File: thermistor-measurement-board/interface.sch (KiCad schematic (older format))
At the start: 12 parts, among them P401 PWR, P402 BIAS, P403 OUT_A, P404 OUT_B, P406 I/O

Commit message: took care of a few board review tasks
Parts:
- added P405: ADC_REF, Pin_Headers:Pin_Header_Straight_1x02, symbol CONN_01X02
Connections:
- new net ADC_REF+: P405.1 (P1)
- new net ADC_REF-: P405.2 (P2)
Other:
- moved on the sheet: P403, P404, P406

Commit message: lots of design review and related fixes/improvements
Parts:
- P405: footprint Pin_Headers:Pin_Header_Straight_1x02 -> Pin_Headers:Pin_Header_Straight_1x04; symbol CONN_01X02 -> CONN_01X04
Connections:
- net ADC_REF+: now also P405.2 (P2)
- net ADC_REF-: now also P405.3 (P3), P405.4 (P4); no longer P405.2 (P2)
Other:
- moved on the sheet: P403, P404, P406
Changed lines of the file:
@@
 	3500 1500 2900 1500
 Wire Wire Line
-	2650 4300 3250 4300
-Wire Wire Line
-	2650 4400 3250 4400
-Wire Wire Line
 	2650 4500 3250 4500
-Text Label 2650 4300 0    60   ~ 0
+Wire Wire Line
+	2650 4600 3250 4600
+Wire Wire Line
+	2650 4700 3250 4700
+Text Label 2650 4500 0    60   ~ 0
 SCLK
-Text Label 2650 4500 0    60   ~ 0
+Text Label 2650 4700 0    60   ~ 0
 MISO
-Text Label 2650 4400 0    60   ~ 0
+Text Label 2650 4600 0    60   ~ 0
 MOSI
-Text Label 3500 2900 2    60   ~ 0
+Text Label 3500 3100 2    60   ~ 0
 OUT_A+
-Text Label 3500 3100 2    60   ~ 0
+Text Label 3500 3300 2    60   ~ 0
 OUT_A-
 Wire Wire Line
-	2900 3100 3500 3100
-Wire Wire Line
-	3500 2900 2900 2900
+	2900 3300 3500 3300
+Wire Wire Line
+	3500 3100 2900 3100
 $Comp
 L GND #PWR038
 U 1 1 56B76BAA
-P 2750 3900
-F 0 "#PWR038" H 2750 3650 50  0001 C CNN
-F 1 "GND" H 2750 3750 50  0000 C CNN
-F 2 "" H 2750 3900 50  0000 C CNN
-F 3 "" H 2750 3900 50  0000 C CNN
-	1    2750 3900
+P 2750 4100
+F 0 "#PWR038" H 2750 3850 50  0001 C CNN
+F 1 "GND" H 2750 3950 50  0000 C CNN
+F 2 "" H 2750 4100 50  0000 C CNN
+F 3 "" H 2750 4100 50  0000 C CNN
+	1    2750 4100
 	0    1    -1   0
 $EndComp
 Wire Wire Line
-	3250 3900 2750 3900
-Wire Wire Line
-	2650 4200 3250 4200
-Text Label 2650 4200 0    60   ~ 0
+	3250 4100 2750 4100
+Wire Wire Line
+	2650 4400 3250 4400
+Text Label 2650 4400 0    60   ~ 0
 MUX_CS
-Text Label 4350 4000 2    60   ~ 0
+Text Label 4350 4200 2    60   ~ 0
 ADC_CS
 Wire Wire Line
-	4350 4000 3750 4000
-Wire Wire Line
-	2650 4100 3250 4100
-Text Label 2650 4100 0    60   ~ 0
+	4350 4200 3750 4200
+Wire Wire Line
+	2650 4300 3250 4300
+Text Label 2650 4300 0    60   ~ 0
 MUX_EN
+Text Label 4350 4300 2    60   ~ 0
+ADC_DR_INT
+Wire Wire Line
+	3750 4300 4350 4300
 Text Label 4350 4100 2    60   ~ 0
-ADC_DR_INT
-Wire Wire Line
-	3750 4100 4350 4100
-Text Label 4350 3900 2    60   ~ 0
 ADC_RST
 Wire Wire Line
-	4350 3900 3750 3900
+	4350 4100 3750 4100
 Text Label 7000 1100 2    60   ~ 0
 AVCC
@@
 Wire Wire Line
 	1700 3500 1100 3500
-Text Label 3500 3400 2    60   ~ 0
+Text Label 3500 3600 2    60   ~ 0
 OUT_B+
-Text Label 3500 3600 2    60   ~ 0
+Text Label 3500 3800 2    60   ~ 0
 OUT_B-
 Wire Wire Line
-	2900 3600 3500 3600
-Wire Wire Line
-	3500 3400 2900 3400
+	2900 3800 3500 3800
+Wire Wire Line
+	3500 3600 2900 3600
 $Comp
 L CONN_01X03 P403
 U 1 1 56B95AC0
-P 2700 3000
-F 0 "P403" H 2700 3200 50  0000 C CNN
-F 1 "OUT_A" V 2800 3000 50  0000 C CNN
-F 2 "Pin_Headers:Pin_Header_Straight_1x03" H 2700 3000 50  0001 C CNN
-F 3 "" H 2700 3000 50  0000 C CNN
-	1    2700 3000
+P 2700 3200
+F 0 "P403" H 2700 3400 50  0000 C CNN
+F 1 "OUT_A" V 2800 3200 50  0000 C CNN
+F 2 "Pin_Headers:Pin_Header_Straight_1x03" H 2700 3200 50  0001 C CNN
+F 3 "" H 2700 3200 50  0000 C CNN
+	1    2700 3200
 	-1   0    0    -1
 $EndComp
@@
 L CONN_01X03 P404
 U 1 1 56B95B06
-P 2700 3500
-F 0 "P404" H 2700 3700 50  0000 C CNN
-F 1 "OUT_B" V 2800 3500 50  0000 C CNN
-F 2 "Pin_Headers:Pin_Header_Straight_1x03" H 2700 3500 50  0001 C CNN
-F 3 "" H 2700 3500 50  0000 C CNN
-	1    2700 3500
+P 2700 3700
+F 0 "P404" H 2700 3900 50  0000 C CNN
+F 1 "OUT_B" V 2800 3700 50  0000 C CNN
+F 2 "Pin_Headers:Pin_Header_Straight_1x03" H 2700 3700 50  0001 C CNN
+F 3 "" H 2700 3700 50  0000 C CNN
+	1    2700 3700
 	-1   0    0    -1
 $EndComp
 Wire Wire Line
-	4350 4200 3750 4200
-Text Label 4350 4200 2    60   ~ 0
+	4350 4400 3750 4400
+Text Label 4350 4400 2    60   ~ 0
 AMP_MUX_CS
 Wire Wire Line
-	4350 4300 3750 4300
-Text Label 4350 4300 2    60   ~ 0
+	4350 4500 3750 4500
+Text Label 4350 4500 2    60   ~ 0
 AMP_MUX_EN
 Wire Wire Line
-	2650 4000 3250 4000
+	2650 4200 3250 4200
 Text HLabel 1100 4300 0    60   Output ~ 0
 AMP_MUX_CS
@@
 L CONN_02X07 P406
 U 1 1 56B9EC32
-P 3500 4200
-F 0 "P406" H 3500 4600 50  0000 C CNN
-F 1 "I/O" V 3500 4200 50  0000 C CNN
-F 2 "Pin_Headers:Pin_Header_Straight_2x07" H 3500 3000 50  0001 C CNN
-F 3 "" H 3500 3000 50  0000 C CNN
-	1    3500 4200
-	1    0    0    -1
-$EndComp
-Text Label 2650 4000 0    60   ~ 0
+P 3500 4400
+F 0 "P406" H 3500 4800 50  0000 C CNN
+F 1 "I/O" V 3500 4400 50  0000 C CNN
+F 2 "Pin_Headers:Pin_Header_Straight_2x07" H 3500 3200 50  0001 C CNN
+F 3 "" H 3500 3200 50  0000 C CNN
+	1    3500 4400
+	1    0    0    -1
+$EndComp
+Text Label 2650 4200 0    60   ~ 0
 ADC_MCLK
 $Comp
 L GND #PWR041
 U 1 1 56B9EE11
-P 4250 4500
-F 0 "#PWR041" H 4250 4250 50  0001 C CNN
-F 1 "GND" H 4250 4350 50  0000 C CNN
-F 2 "" H 4250 4500 50  0000 C CNN
-F 3 "" H 4250 4500 50  0000 C CNN
-	1    4250 4500
+P 4250 4700
+F 0 "#PWR041" H 4250 4450 50  0001 C CNN
+F 1 "GND" H 4250 4550 50  0000 C CNN
+F 2 "" H 4250 4700 50  0000 C CNN
+F 3 "" H 4250 4700 50  0000 C CNN
+	1    4250 4700
 	0    -1   1    0
 $EndComp
 Wire Wire Line
-	3750 4500 4250 4500
-Text Label 4350 4400 2    60   ~ 0
+	3750 4700 4250 4700
+Text Label 4350 4600 2    60   ~ 0
 DVDD
 Wire Wire Line
-	4350 4400 3750 4400
+	4350 4600 3750 4600
 $Comp
 L PWR_FLAG #FLG042
@@
 Wire Wire Line
 	1700 2600 1100 2600
-Text Label 3500 3500 2    60   ~ 0
+Text Label 3500 3700 2    60   ~ 0
 REF_B
-Text Label 3500 3000 2    60   ~ 0
+Text Label 3500 3200 2    60   ~ 0
 REF_A
 Wire Wire Line
-	3500 3500 2900 3500
-Wire Wire Line
-	3500 3000 2900 3000
+	3500 3700 2900 3700
+Wire Wire Line
+	3500 3200 2900 3200
 Text Label 1700 1800 2    60   ~ 0
 VS_BIAS
@@
 	1700 2900 1100 2900
 $Comp
-L CONN_01X02 P405
+L CONN_01X04 P405
 U 1 1 56BCEDCB
-P 2700 2450
-F 0 "P405" H 2700 2600 50  0000 C CNN
-F 1 "ADC_REF" V 2800 2450 50  0000 C CNN
-F 2 "Pin_Headers:Pin_Header_Straight_1x02" H 2700 2450 50  0001 C CNN
-F 3 "" H 2700 2450 50  0000 C CNN
-	1    2700 2450
+P 2700 2550
+F 0 "P405" H 2700 2800 50  0000 C CNN
+F 1 "ADC_REF" V 2800 2550 50  0000 C CNN
+F 2 "Pin_Headers:Pin_Header_Straight_1x04" H 2700 2550 50  0001 C CNN
+F 3 "" H 2700 2550 50  0000 C CNN
+	1    2700 2550
 	-1   0    0    -1
 $EndComp
 Text Label 3500 2400 2    60   ~ 0
 ADC_REF+
-Text Label 3500 2500 2    60   ~ 0
+Text Label 3500 2700 2    60   ~ 0
 ADC_REF-
 Wire Wire Line
-	3500 2400 2900 2400
-Wire Wire Line
-	2900 2500 3500 2500
+	2900 2500 3000 2500
+Wire Wire Line
+	3000 2500 3000 2400
+Connection ~ 3000 2400
+Wire Wire Line
+	2900 2600 3000 2600
+Wire Wire Line
+	3000 2600 3000 2700
+Connection ~ 3000 2700
+Wire Wire Line
+	2900 2400 3500 2400
+Wire Wire Line
+	2900 2700 3500 2700
 $EndSCHEMATC

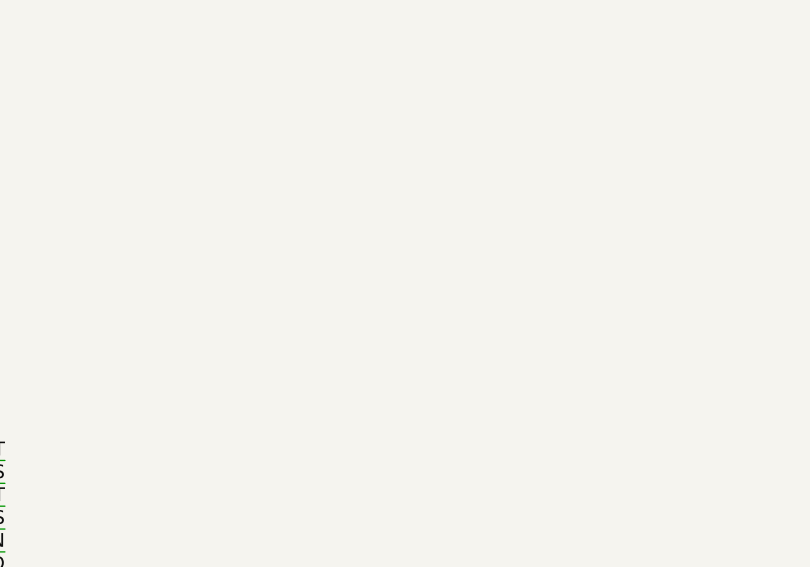
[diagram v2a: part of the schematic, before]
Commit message: read a million instrument amp datasheets and found one that should work nicely for low gain.
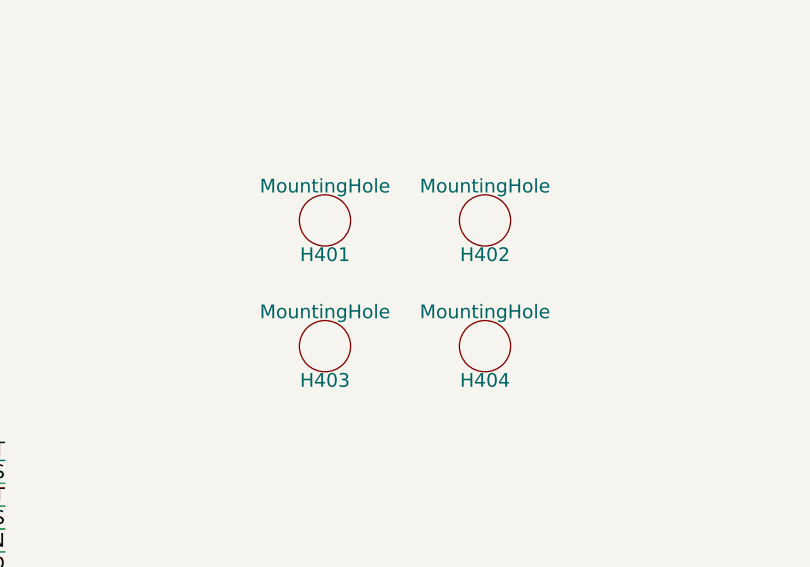
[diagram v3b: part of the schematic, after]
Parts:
- added H401, H402, H403, H404: MountingHole, MountingHole_2-5mm, symbol MountingHole
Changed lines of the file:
@@
 $Descr A4 11693 8268
 encoding utf-8
-Sheet 4 4
+Sheet 4 5
 Title ""
 Date ""
@@
 	1100 800  1700 800
 $Comp
-L GND #PWR033
+L GND #PWR035
 U 1 1 56B64614
 P 1700 1400
-F 0 "#PWR033" H 1700 1150 50  0001 C CNN
+F 0 "#PWR035" H 1700 1150 50  0001 C CNN
 F 1 "GND" H 1700 1250 50  0000 C CNN
 F 2 "" H 1700 1400 50  0000 C CNN
@@
 $EndComp
 $Comp
-L GNDA #PWR034
+L GNDA #PWR036
 U 1 1 56B6461A
 P 1700 1600
-F 0 "#PWR034" H 1700 1350 50  0001 C CNN
+F 0 "#PWR036" H 1700 1350 50  0001 C CNN
 F 1 "GNDA" H 1700 1450 50  0000 C CNN
 F 2 "" H 1700 1600 50  0000 C CNN
@@
 $EndComp
 $Comp
-L GND #PWR035
+L GND #PWR037
 U 1 1 56B765F3
 P 5200 1600
-F 0 "#PWR035" H 5200 1350 50  0001 C CNN
+F 0 "#PWR037" H 5200 1350 50  0001 C CNN
 F 1 "GND" H 5200 1450 50  0000 C CNN
 F 2 "" H 5200 1600 50  0000 C CNN
@@
 $EndComp
 $Comp
-L GNDA #PWR036
+L GNDA #PWR038
 U 1 1 56B7660A
 P 6100 1600
-F 0 "#PWR036" H 6100 1350 50  0001 C CNN
+F 0 "#PWR038" H 6100 1350 50  0001 C CNN
 F 1 "GNDA" H 6100 1450 50  0000 C CNN
 F 2 "" H 6100 1600 50  0000 C CNN
@@
 	3300 800  2900 800
 $Comp
-L GNDA #PWR037
+L GNDA #PWR039
 U 1 1 56B767B9
 P 3400 1400
-F 0 "#PWR037" H 3400 1150 50  0001 C CNN
+F 0 "#PWR039" H 3400 1150 50  0001 C CNN
 F 1 "GNDA" H 3400 1250 50  0000 C CNN
 F 2 "" H 3400 1400 50  0000 C CNN
@@
 	3500 3100 2900 3100
 $Comp
-L GND #PWR038
+L GND #PWR040
 U 1 1 56B76BAA
 P 2750 4100
-F 0 "#PWR038" H 2750 3850 50  0001 C CNN
+F 0 "#PWR040" H 2750 3850 50  0001 C CNN
 F 1 "GND" H 2750 3950 50  0000 C CNN
 F 2 "" H 2750 4100 50  0000 C CNN
@@
 	6100 1400 6100 1600
 $Comp
-L GND #PWR039
+L GND #PWR041
 U 1 1 56B76F43
 P 3200 900
-F 0 "#PWR039" H 3200 650 50  0001 C CNN
+F 0 "#PWR041" H 3200 650 50  0001 C CNN
 F 1 "GND" H 3200 750 50  0000 C CNN
 F 2 "" H 3200 900 50  0000 C CNN
@@
 $EndComp
 $Comp
-L GNDA #PWR040
+L GNDA #PWR042
 U 1 1 56B76F8A
 P 3350 1000
-F 0 "#PWR040" H 3350 750 50  0001 C CNN
+F 0 "#PWR042" H 3350 750 50  0001 C CNN
 F 1 "GNDA" H 3350 850 50  0000 C CNN
 F 2 "" H 3350 1000 50  0000 C CNN
@@
 ADC_MCLK
 $Comp
-L GND #PWR041
+L GND #PWR043
 U 1 1 56B9EE11
 P 4250 4700
-F 0 "#PWR041" H 4250 4450 50  0001 C CNN
+F 0 "#PWR043" H 4250 4450 50  0001 C CNN
 F 1 "GND" H 4250 4550 50  0000 C CNN
 F 2 "" H 4250 4700 50  0000 C CNN
@@
 	4350 4600 3750 4600
 $Comp
-L PWR_FLAG #FLG042
+L PWR_FLAG #FLG044
 U 1 1 56B9EF5B
 P 6600 1000
-F 0 "#FLG042" H 6600 1095 50  0001 C CNN
+F 0 "#FLG044" H 6600 1095 50  0001 C CNN
 F 1 "PWR_FLAG" H 6600 1180 50  0000 C CNN
 F 2 "" H 6600 1000 50  0000 C CNN
@@
 	2900 1900 3500 1900
 $Comp
-L PWR_FLAG #FLG043
+L PWR_FLAG #FLG045
 U 1 1 56BB4BA6
 P 7800 1000
-F 0 "#FLG043" H 7800 1095 50  0001 C CNN
+F 0 "#FLG045" H 7800 1095 50  0001 C CNN
 F 1 "PWR_FLAG" H 7800 1180 50  0000 C CNN
 F 2 "" H 7800 1000 50  0000 C CNN
@@
 VS_BIAS
 $Comp
-L GNDA #PWR044
+L GNDA #PWR046
 U 1 1 56BB4CC1
 P 7800 1500
-F 0 "#PWR044" H 7800 1250 50  0001 C CNN
+F 0 "#PWR046" H 7800 1250 50  0001 C CNN
 F 1 "GNDA" H 7800 1350 50  0000 C CNN
 F 2 "" H 7800 1500 50  0000 C CNN
@@
 Wire Wire Line
 	2900 2700 3500 2700
+$Comp
+L MountingHole H401
+U 1 1 56C191B5
+P 5750 3050
+F 0 "H401" H 5750 2900 60  0000 C CNN
+F 1 "MountingHole" H 5750 3200 60  0000 C CNN
+F 2 "MountingHole_2-5mm" H 5750 3050 60  0001 C CNN
+F 3 "" H 5750 3050 60  0000 C CNN
+	1    5750 3050
+	1    0    0    -1
+$EndComp
+$Comp
+L MountingHole H402
+U 1 1 56C19288
+P 6450 3050
+F 0 "H402" H 6450 2900 60  0000 C CNN
+F 1 "MountingHole" H 6450 3200 60  0000 C CNN
+F 2 "MountingHole_2-5mm" H 6450 3050 60  0001 C CNN
+F 3 "" H 6450 3050 60  0000 C CNN
+	1    6450 3050
+	1    0    0    -1
+$EndComp
+$Comp
+L MountingHole H403
+U 1 1 56C192CF
+P 5750 3600
+F 0 "H403" H 5750 3450 60  0000 C CNN
+F 1 "MountingHole" H 5750 3750 60  0000 C CNN
+F 2 "MountingHole_2-5mm" H 5750 3600 60  0001 C CNN
+F 3 "" H 5750 3600 60  0000 C CNN
+	1    5750 3600
+	1    0    0    -1
+$EndComp
+$Comp
+L MountingHole H404
+U 1 1 56C19319
+P 6450 3600
+F 0 "H404" H 6450 3450 60  0000 C CNN
+F 1 "MountingHole" H 6450 3750 60  0000 C CNN
+F 2 "MountingHole_2-5mm" H 6450 3600 60  0001 C CNN
+F 3 "" H 6450 3600 60  0000 C CNN
+	1    6450 3600
+	1    0    0    -1
+$EndComp
 $EndSCHEMATC
